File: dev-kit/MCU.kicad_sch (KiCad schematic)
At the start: 33 parts, among them IC302 FAN5622SX, IC303 MX25U51245GZ4I00, IC305 NTS0104GU12, IC306 DRV2603RUNT, IC307 RV-8263-C8, M301 NORA-B106, M302 Vibrator DC Motor, Q301 BC817W, Q302 PMZ550UNEYL, Q303 PMZ550UNEYL, X302 GC9A01A_CST816S, X303 M+, X304 M-

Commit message: PCB: Add new vibration motor
- Remove old hardware project (comes back later)
- Add new dev-kit project

Closes #102

Signed-off-by: Daniel Kampert <danielkampert@kampis-elektroecke.de>
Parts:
- removed X303: M+, TestPoint:TestPoint_Pad_1.0x1.0mm, symbol Connector_Generic:Conn_01x01
- removed X304: M-, TestPoint:TestPoint_Pad_1.0x1.0mm, symbol Connector_Generic:Conn_01x01
- added X102: MOTOR, Molex:78171-0002, symbol Connector_Generic:Conn_01x02
- BZ301, C301, C302, C304, C305, C306, C307, D301, IC302, IC303, IC305, IC306, IC307, M301, Q301, Q302, Q303, R301, R302, R303, R304, R307, R309, R311, R313, S301, S302, S303, S304: Distributor Mouser -> (none)
- M302: Distributor Mouser -> (none); digikey# (none) -> 1670-VC1027B902F-ND; manf DFRobot -> Vybronics Inc; manf# FIT0774 -> VC1027B902F; mouser# 426-FIT0774 -> (none)
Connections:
- net at IC306.9 (OUT+): now also X102.1 (Pin_1); no longer M302.1 (+)
- net at IC306.6 (OUT-): now also X102.2 (Pin_2); no longer M302.2 (-)
- no-connect marks 16 -> 18
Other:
- title: ZSWatch v3 -> ZSWatch v3 Dev-Kit
- moved on the sheet: M302

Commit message: Add 0805 resistors for current measurement, reorganize schematics
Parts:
- removed BZ301: Buzzer, CUI Devices:CMT-322-65-SMT-TR, symbol Device:Buzzer
- removed C306: 100n, Capacitor_SMD:C_0603_1608Metric, symbol Device:C_Small
- removed C307: 100n, Capacitor_SMD:C_0402_1005Metric, symbol Device:C_Small
- removed D301: BAS316, Diode_SMD:D_SOD-323, symbol Diode:BAS316
- removed IC306: DRV2603RUNT, Package_QFN:WQFN-10_2x2mm_P0.5mm, symbol TexasInstruments_Kampi:DRV2603RUNT
- removed IC307: RV-8263-C8, Micro Crystal:RV-8263-C8, symbol Micro Crystal:RV-8263-C8
- removed M302: Vibrator DC Motor, symbol Motor:Motor_DC
- removed Q301: BC817W, Package_TO_SOT_SMD:SOT-323_SC-70, symbol Transistor_BJT:BC817W
- removed Q302, Q303: PMZ550UNEYL, Package_SOT_SMD:SOT-883, symbol Nexperia:PMZ550UNEYL
- removed R303, R304: 4k7, Resistor_SMD:R_0603_1608Metric, symbol Device:R_Small
- removed R307: 150k, Resistor_SMD:R_0603_1608Metric, symbol Device:R_Small
- removed R309, R313: 4k7, Resistor_SMD:R_0402_1005Metric, symbol Device:R_Small
- removed R311: 180R, Resistor_SMD:R_0603_1608Metric, symbol Device:R_Small
- removed S301: SW1, E-Switch:TL6340AF160Q_Modified, symbol Switch:SW_Push
- removed S302: SW2, E-Switch:TL6340AF160Q_Modified, symbol Switch:SW_Push
- removed S303: SW3, E-Switch:TL6340AF160Q_Modified, symbol Switch:SW_Push
- removed S304: SW4, E-Switch:TL6340AF160Q_Modified, symbol Switch:SW_Push
- removed X102: MOTOR, Molex:78171-0002, symbol Connector_Generic:Conn_01x02
- added IC107: USBLC6-2P6, Package_TO_SOT_SMD:SOT-666, symbol Power_Protection:USBLC6-2P6
- added R104, R105, R110, R113, R114, R115, R117, R118, R126, R127: 0R, Resistor_SMD:R_0805_2012Metric, symbol Device:R_Small
- added R111, R112: 5k1, Resistor_SMD:R_0402_1005Metric, symbol Device:R_Small
- added TP104: SDA, TestPoint:TestPoint_Pad_D1.0mm, symbol Connector:TestPoint
- added TP105: SCL, TestPoint:TestPoint_Pad_D1.0mm, symbol Connector:TestPoint
- added TP108: TxD, TestPoint:TestPoint_Pad_D1.0mm, symbol Connector:TestPoint
- added TP109: RxD, TestPoint:TestPoint_Pad_D1.0mm, symbol Connector:TestPoint
- added TP110: MCU Reset, TestPoint:TestPoint_Pad_D1.0mm, symbol Connector:TestPoint
- added X103: Device, Connector_USB:USB_C_Receptacle_GCT_USB4105-xx-A_16P_TopMnt_Horizontal, symbol Connector:USB_C_Receptacle
- C301: footprint Capacitor_SMD:C_0603_1608Metric -> Capacitor_SMD:C_0402_1005Metric; CONFIG -ENV -> (none); manf# 0603YC105JAT2A -> 04023D105KAT2A; mouser# 581-0603YC105JAT2A -> 581-04023D105KAT2A
- C302: footprint Capacitor_SMD:C_0603_1608Metric -> Capacitor_SMD:C_0402_1005Metric; manf# 06035C104KAT2A -> 0402ZC104KAT4A; mouser# 581-06035C104KAT2A -> 581-0402ZC104KAT4A
- C304, C305: footprint Capacitor_SMD:C_0603_1608Metric -> Capacitor_SMD:C_0402_1005Metric; CONFIG -ENV -> (none); manf# 06035C104KAT2A -> 0402ZC104KAT4A; mouser# 581-06035C104KAT2A -> 581-0402ZC104KAT4A
- IC302, IC305, X302: CONFIG -ENV -> (none)
- R301: footprint Resistor_SMD:R_0603_1608Metric -> Resistor_SMD:R_0402_1005Metric; CONFIG -ENV -> (none); manf# RC0603FR-0712KL -> RC0402FR-0712KL; mouser# 603-RC0603FR-0712KL -> 603-RC0402FR-0712KL
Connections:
- net BTN-1 is gone; now on net SW1: M301.H3 (P0.27/AIN6)
- net +1V8: now also R110.2, R113.2, R117.2, R127.1; no longer C302.1, C304.1, IC303.8 (VCC), IC305.1 (VCCA), M301.A7 (VDD), M301.A8 (VDDH), M301.B7 (VDD), X302.11 (VDDIO), X302.12 (VDDIO)
- net +3V0: now also R114.2, R115.1, R118.2, R126.1
- net GND: now also C302.1, IC107.2 (GND), R111.2, R112.1, X103.A1 (GND), X103.A12 (GND), X103.B1 (GND), X103.B12 (GND), X103.S1 (SHIELD); no longer C302.2
- net RESETn: now also TP110.1, X103.A8 (SBU1), X103.B8 (SBU2)
- net SWDCLK: now also X103.A11 (RX2+), X103.B11 (RX1+)
- net SWDIO: now also X103.A10 (RX2-), X103.B10 (RX1-)
- net TOUCH-INT: now also IC305.2 (A1); no longer IC305.3 (A2)
- net TOUCH-SCL: now also IC305.3 (A2); no longer IC305.2 (A1)
- net at IC305.10 (B1): now also X302.21 (CTP-INT); no longer X302.20 (CTP-SCL)
- net at IC305.9 (B2): now also X302.20 (CTP-SCL); no longer X302.21 (CTP-INT)
- net SW1: now reaches M301.H8 (P0.30)
- net TxD: now reaches M301.G8 (P1.12)
- net TxD: now also TP108.1, X103.A3 (TX1-), X103.B3 (TX2-)
- net RxD: now reaches M301.H9 (P1.11)
- net RxD: now also TP109.1, X103.A2 (TX1+), X103.B2 (TX2+)
- net BTN-2: no longer names the net of M301.J7 (P1.10)
- net BTN-3 renamed SW3
- net BTN-4 renamed SW4
- net SENSOR-SCL renamed SCL
- net SCL: now also TP105.1
- net SENSOR-SDA renamed SDA
- net SDA: now also TP104.1
- net USB-D_N renamed USB-D-
- net USB-D-: now also IC107.6 (I/O1)
- net USB-D_P renamed USB-D+
- net USB-D+: now also IC107.4 (I/O2)
- net VBUS-MCU renamed USB-VBUS-Out
- removed net VDD-Display: C301.2, C305.1, IC302.3 (VIN), IC305.11 (VCCB), X302.13 (VDD), X302.14 (VDD), X302.17 (CTP-VDD), X302.23 (LEDA2), X302.24 (LEDA1)
- new net: IC107.1 (I/O1), X103.A7 (D-), X103.B7 (D-)
- new net: IC107.3 (I/O2), X103.A6 (D+), X103.B6 (D+)
- new net: M301.A7 (VDD), M301.A8 (VDDH), M301.B7 (VDD), R110.1
- new net: C304.1, IC305.1 (VCCA), R117.1
- new net: C305.1, IC305.11 (VCCB), R118.1
- new net: R105.1, X103.A5 (CC1)
- new net: R104.2, X103.B5 (CC2)
- new net: C301.2, IC302.3 (VIN), R126.2
- new net: R113.1, X302.11 (VDDIO), X302.12 (VDDIO)
- new net: R114.1, X302.13 (VDD), X302.14 (VDD), X302.17 (CTP-VDD)
- new net: R115.2, X302.23 (LEDA2), X302.24 (LEDA1)
- new net: C302.2, IC303.8 (VCC), R127.2
- new net CC1: R105.2, R112.2
- new net CC2: R104.1, R111.1
- new net USB-VBUS-In: IC107.5 (VBUS), X103.A4 (VBUS), X103.A9 (VBUS), X103.B4 (VBUS), X103.B9 (VBUS)
- no-connect marks 18 -> 12
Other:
- note added: "From transmitter"
- note added: "NOTE: 1V8 <-> 3V0 level shifter NTS0104GU12 has internal pullups. Works for I2C. https://www.nxp.com/docs/en/data-sheet/NTS0104.pdf"
- note added: "To receiver"
- note added: "USB"
- note removed: "Buttons"
- note removed: "Buzzer"
- note removed: "NOTE: 1V8 <-> 3V3 level shifter NTS0104GU12 has internal pullups. Works for I2C. https://www.nxp.com/docs/en/data-sheet/NTS0104.pdf"
- note removed: "NOTE: CLKOUT is disabled."
- note removed: "NOTE: Configured for ERM mode."
- note removed: "RTC"
- note removed: "Vibration motor"
- moved on the sheet: C301, C304, C305, IC302, IC303, IC305, M301A, M301B, M301C, R302, X302

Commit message: Working on the layout for the dev kit
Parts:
- added R106, R107, R128, R129, R130: 0R, Resistor_SMD:R_0805_2012Metric, symbol Device:R_Small
- added X104: DEBUG, Connector_PinHeader_1.27mm:PinHeader_2x05_P1.27mm_Vertical, symbol Connector:Conn_ARM_JTAG_SWD_10
- IC302: footprint Package_TO_SOT_SMD:TSOT-23-6 -> Package_DFN_QFN:UQFN-10_1.4x1.8mm_P0.4mm; symbol ON Semiconductor:FAN5622SX -> ON Semiconductor:FAN5624; manf# FAN5622SX -> FAN5624UMPX; mouser# 512-FAN5622SX -> 512-FAN5624UMPX
- R302: footprint Resistor_SMD:R_0603_1608Metric -> Resistor_SMD:R_0402_1005Metric; manf# RC0603FR-07100KL -> RC0404FR-07100KL; mouser# 603-RC0603FR-07100KL -> 603-RC0404FR-07100KL
- X103: footprint Connector_USB:USB_C_Receptacle_GCT_USB4105-xx-A_16P_TopMnt_Horizontal -> Connector_USB:USB_C_Receptacle_Amphenol_12401610E4-2A; manf GCT -> Amphenol Commercial Products; manf# USB4105-GF-A -> 12401610E4-2A; mouser# 640-USB4105-GF-A -> 523-12401610E4#2A
- X302: value GC9A01A_CST816S -> Display
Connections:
- net nRTC-INT is gone; now on net PMIC-INT: M301.G9 (P1.13)
- net +1V8: now also X104.1 (VTref)
- net BUZZER: no longer M301.B6 (P0.01/XL2)
- net CC1: no longer R112.2
- net CC2: no longer R111.1
- net DISPLAY-BLK: now also IC302.7 (CTRL); no longer IC302.1 (CTRL)
- net DISPLAY-CLK: now also M301.A4 (P1.00); no longer M301.B1 (P0.08/TRACEDATA[3])
- net DISPLAY-CS: now also M301.A5 (P0.20); no longer M301.A2 (P0.12/TRACECLK)
- net DISPLAY-DATA: now also M301.A3 (P1.03/I2C); no longer M301.C2 (P0.09/TRACEDATA[2])
- net DISPLAY-DC: now also M301.D3 (P0.07/AIN3); no longer M301.B3 (P0.11/TRACEDATA[0])
- net DISPLAY-EN: now also M301.B3 (P0.11/TRACEDATA[0]); no longer M301.C4 (P1.01)
- net GND: now also IC302.6 (GND), X104.3 (GND), X104.5 (GND); no longer IC302.2 (GND)
- net LEDK1: now also IC302.8 (LED1); no longer IC302.6 (LED1)
- net LEDK2: now also IC302.10 (LED2); no longer IC302.4 (LED2)
- net LIS2MDL-INT: now also M301.C2 (P0.09/TRACEDATA[2]); no longer M301.H1 (P0.24)
- net MIC-CLK: now also M301.C6 (P0.00/XL1); no longer M301.F3 (P0.19)
- net MIC-DATA: now also M301.B6 (P0.01/XL2); no longer M301.G3 (P0.25/AIN4)
- net MIC-EN: now also M301.E3 (P0.21); no longer M301.G1 (P1.06)
- net PMIC-INT: no longer M301.J8 (P0.28/AIN7)
- net RESETn: now also R130.1, X104.10 (~{RESET}); no longer X103.A8 (SBU1), X103.B8 (SBU2)
- net RxD: now also R128.1; no longer X103.A2 (TX1+), X103.B2 (TX2+)
- net SCL: now also M301.G3 (P0.25/AIN4); no longer M301.D3 (P0.07/AIN3)
- net SDA: now also M301.H3 (P0.27/AIN6); no longer M301.C1 (P0.10/TRACEDATA[1])
- net SW1: now also M301.F3 (P0.19); no longer M301.H3 (P0.27/AIN6), M301.H8 (P0.30)
- net SW3: now also M301.G1 (P1.06); no longer M301.J9 (P0.31)
- net SW4: now also M301.H1 (P0.24); no longer M301.G2 (P0.26/AIN5)
- net SWDCLK: now also R107.1, X104.4 (SWCLK/TCK); no longer X103.A11 (RX2+), X103.B11 (RX1+)
- net SWDIO: now also R106.1, X104.2 (SWDIO/TMS); no longer X103.A10 (RX2-), X103.B10 (RX1-)
- net TOUCH-INT: now also M301.B4 (P1.02/I2C); no longer M301.A4 (P1.00)
- net TOUCH-RST: now also M301.E7 (P0.06/AIN2); no longer M301.A5 (P0.20)
- net TOUCH-SCL: now also M301.C4 (P1.01); no longer M301.A3 (P1.03/I2C)
- net TOUCH-SDA: now also M301.C5 (P0.02/NFC1); no longer M301.B4 (P1.02/I2C)
- net TxD: now also R129.1; no longer X103.A3 (TX1-), X103.B3 (TX2-)
- net VIB-EN: now also M301.E9 (P1.05); no longer M301.F9 (P1.15)
- net VIB-PWM: now also M301.F9 (P1.15); no longer M301.E9 (P1.05)
- net at X103.A7 (D-), X103.B7 (D-): now also IC107.3 (I/O2); no longer IC107.1 (I/O1)
- net at X103.A6 (D+), X103.B6 (D+): now also IC107.1 (I/O1); no longer IC107.3 (I/O2)
- net at R105.1, X103.A5 (CC1): now also R111.1
- net at R104.2, X103.B5 (CC2): now also R112.2
- net at C301.2, R126.2: now also IC302.5 (VIN); no longer IC302.3 (VIN)
- net at R301.2: now also IC302.3 (ISET); no longer IC302.5 (ISET)
- net BMI270-INT1: no longer names the net of M301.G5 (P1.08)
- net BMI270-INT2: no longer names the net of M301.G4 (P1.04)
- new net: R107.2, X103.A11 (RX2+), X103.B11 (RX1+)
- new net: R130.2, X103.A8 (SBU1), X103.B8 (SBU2)
- new net: IC302.4 (NC), IC302.9 (NC)
- new net: R106.2, X103.A10 (RX2-), X103.B10 (RX1-)
- new net: R128.2, X103.A2 (TX1+), X103.B2 (TX2+)
- new net: R129.2, X103.A3 (TX1-), X103.B3 (TX2-)
- new net APDS-INT: M301.C1 (P0.10/TRACEDATA[1])
- new net BMI270-INT: M301.B1 (P0.08/TRACEDATA[3])
- new net SW2: M301.G2 (P0.26/AIN5)
- new net ~{RTC-INT}: M301.A2 (P0.12/TRACECLK)
- no-connect marks 12 -> 19
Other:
- note added: "Debug connector"
- moved on the sheet: C301, R111, R112, R126, TP104, TP105

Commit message: Add more documentation
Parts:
- removed R110, R113, R114, R115, R127: 0R, Resistor_SMD:R_0805_2012Metric, symbol Device:R_Small
- added X207, X208: Power, Connector_PinHeader_2.54mm:PinHeader_1x02_P2.54mm_Vertical_SMD_Pin1Left, symbol Connector_Generic:Conn_01x02
- added X209: LED Power, Connector_PinHeader_2.54mm:PinHeader_1x02_P2.54mm_Vertical_SMD_Pin1Left, symbol Connector_Generic:Conn_01x02
- added X210: Touch Power, Connector_PinHeader_2.54mm:PinHeader_1x02_P2.54mm_Vertical_SMD_Pin1Left, symbol Connector_Generic:Conn_01x02
- added X211: IO Power, Connector_PinHeader_2.54mm:PinHeader_1x02_P2.54mm_Vertical_SMD_Pin1Left, symbol Connector_Generic:Conn_01x02
- TP110: value MCU Reset -> Reset
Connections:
- net +1V8: now also X207.2 (Pin_2), X208.2 (Pin_2), X211.2 (Pin_2)
- net +3V0: now also X209.1 (Pin_1), X210.1 (Pin_1)
- net BMI270-INT: now also M301.A2 (P0.12/TRACECLK); no longer M301.B1 (P0.08/TRACEDATA[3])
- net DISPLAY-CLK: now also M301.C2 (P0.09/TRACEDATA[2]); no longer M301.A4 (P1.00)
- net DISPLAY-DATA: now also M301.B1 (P0.08/TRACEDATA[3]); no longer M301.A3 (P1.03/I2C)
- net DISPLAY-DC: now also M301.A4 (P1.00); no longer M301.D3 (P0.07/AIN3)
- net LIS2MDL-INT: now also M301.E3 (P0.21); no longer M301.C2 (P0.09/TRACEDATA[2])
- net MIC-EN: now also M301.D3 (P0.07/AIN3); no longer M301.E3 (P0.21)
- net ~{RTC-INT}: now also M301.A3 (P1.03/I2C); no longer M301.A2 (P0.12/TRACECLK)
- net at M301.A7 (VDD), M301.A8 (VDDH), M301.B7 (VDD): now also X207.1 (Pin_1)
- net at X302.11 (VDDIO), X302.12 (VDDIO): now also X211.1 (Pin_1)
- net at X302.13 (VDD), X302.14 (VDD), X302.17 (CTP-VDD): now also X210.2 (Pin_2)
- net at X302.23 (LEDA2), X302.24 (LEDA1): now also X209.2 (Pin_2)
- net at C302.2, IC303.8 (VCC): now also X208.1 (Pin_1)

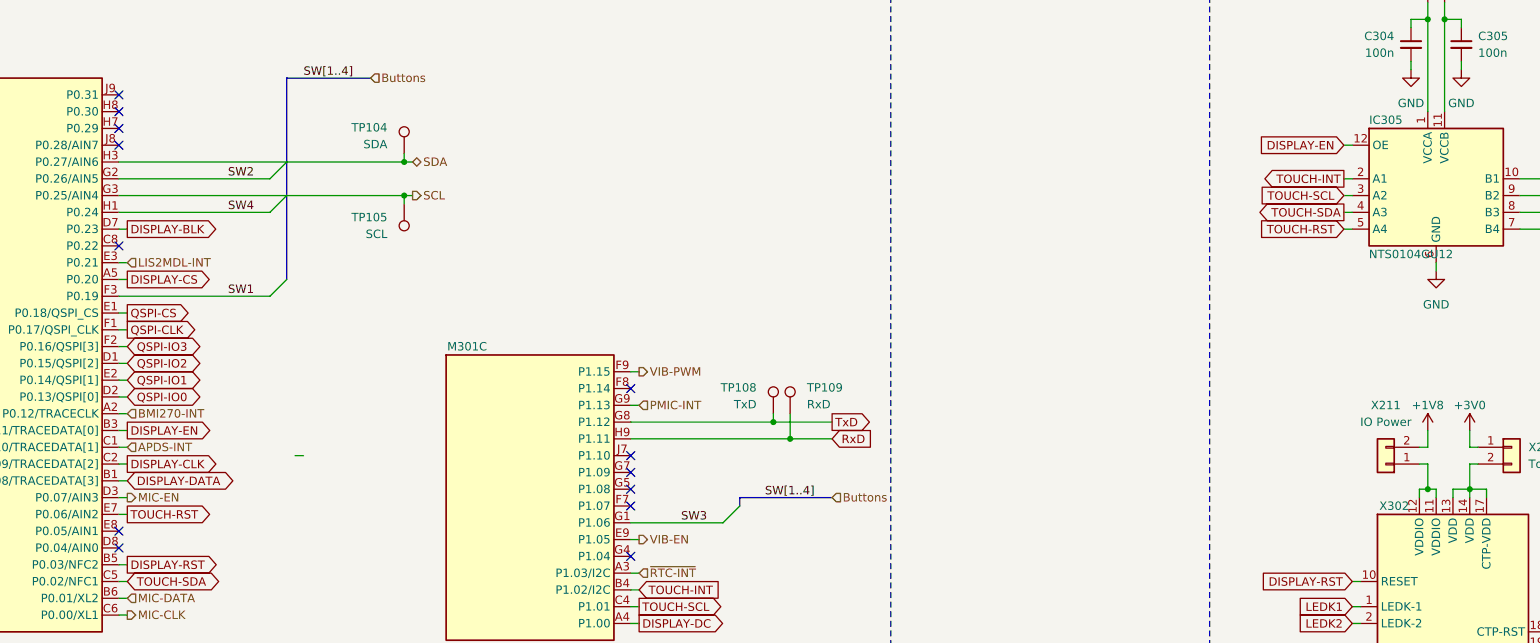
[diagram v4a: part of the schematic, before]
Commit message: Add CI/CD pipeline for Dev-Kit, more Dev-Kit improvements
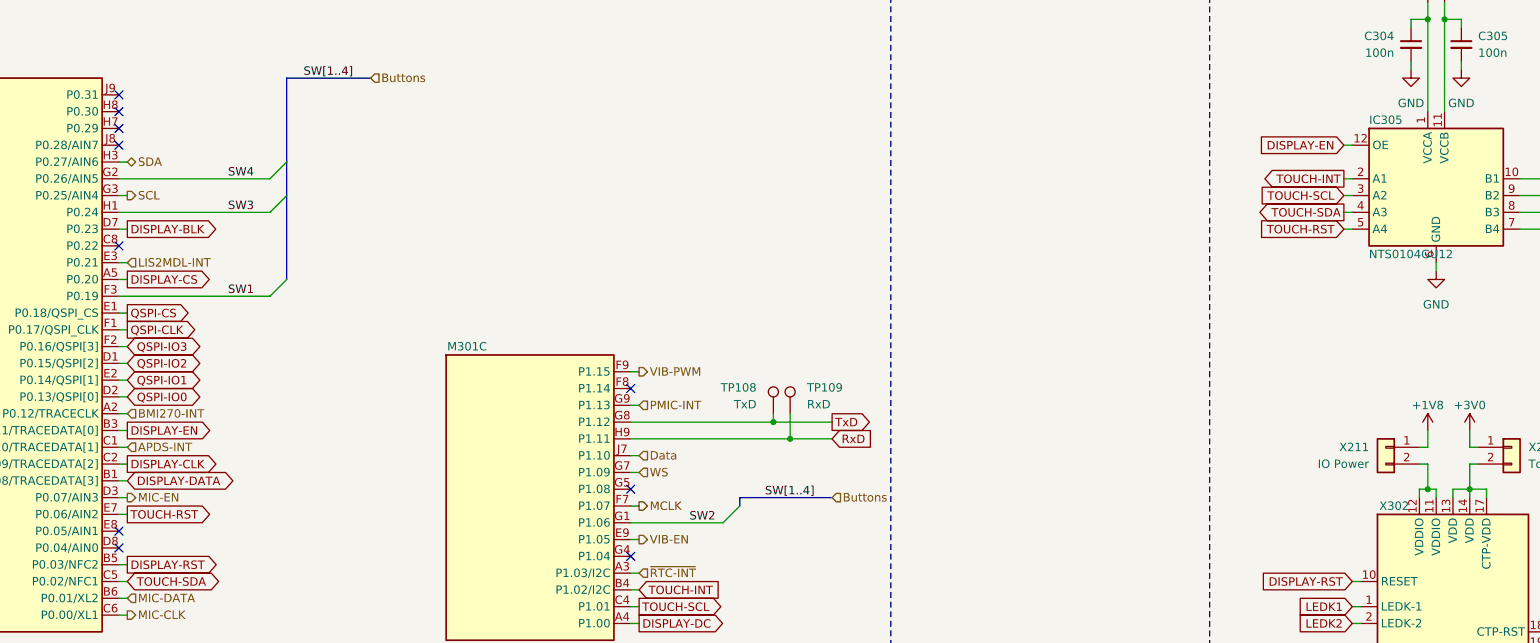
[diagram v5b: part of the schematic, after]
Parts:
- removed TP104: SDA, TestPoint:TestPoint_Pad_D1.0mm, symbol Connector:TestPoint
- removed TP105: SCL, TestPoint:TestPoint_Pad_D1.0mm, symbol Connector:TestPoint
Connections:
- net +1V8: now also X211.1 (Pin_1); no longer X211.2 (Pin_2)
- net SW2: now also M301.G1 (P1.06); no longer M301.G2 (P0.26/AIN5)
- net SW3: now also M301.H1 (P0.24); no longer M301.G1 (P1.06)
- net SW4: now also M301.G2 (P0.26/AIN5); no longer M301.H1 (P0.24)
- net at X302.11 (VDDIO), X302.12 (VDDIO): now also X211.2 (Pin_2); no longer X211.1 (Pin_1)
- net MCLK: now reaches M301.F7 (P1.07)
- net WS: now reaches M301.G7 (P1.09)
- net Data: now reaches M301.J7 (P1.10)
- no-connect marks 19 -> 16
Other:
- moved on the sheet: X211
